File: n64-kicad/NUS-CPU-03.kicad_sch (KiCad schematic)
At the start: 1 part

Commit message: Update
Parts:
- added U4: ~, symbol n64:VDC-NUS
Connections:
- net +3V3: now also U4.1 (3V3)
- net GND: now also U4.12 (VSS), U4.9 (VSS)
- net at U1.11 (VIDEO_CLK): now also U4.11 (CLOCK)
- net at U1.14 (VIDEO_SYNC): now also U4.10 (~{DSYNC})
- net at U1.15 (VIDEO_D6): now also U4.8 (D6)
- net at U1.18 (VIDEO_D5): now also U4.7 (D5)
- net at U1.19 (VIDEO_D4): now also U4.6 (D4)
- net at U1.20 (VIDEO_D3): now also U4.5 (D3)
- net at U1.23 (VIDEO_D2): now also U4.4 (D2)
- net at U1.24 (VIDEO_D1): now also U4.3 (D1)
- net at U1.25 (VIDEO_D0): now also U4.2 (D0)
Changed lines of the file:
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@@
   (junction (at 165.1 93.98) (diameter 0) (color 0 0 0 0)
   )
+  (junction (at 219.71 124.46) (diameter 0) (color 0 0 0 0)
+  )
   (junction (at 157.48 160.02) (diameter 0) (color 0 0 0 0)
   )
@@
   (junction (at 162.56 86.36) (diameter 0) (color 0 0 0 0)
   )
+  (wire (pts (xy 190.5 116.84) (xy 190.5 111.76))
+    (stroke (width 0) (type default))
+  )
   (wire (pts (xy 165.1 88.9) (xy 165.1 93.98))
     (stroke (width 0) (type default))
   )
+  (wire (pts (xy 157.48 111.76) (xy 180.34 111.76))
+    (stroke (width 0) (type default))
+  )
+  (wire (pts (xy 195.58 124.46) (xy 157.48 124.46))
+    (stroke (width 0) (type default))
+  )
   (wire (pts (xy 157.48 91.44) (xy 162.56 91.44))
     (stroke (width 0) (type default))
@@
     (stroke (width 0) (type default))
   )
+  (wire (pts (xy 219.71 96.52) (xy 222.25 96.52))
+    (stroke (width 0) (type default))
+  )
   (wire (pts (xy 157.48 106.68) (xy 165.1 106.68))
     (stroke (width 0) (type default))
@@
     (stroke (width 0) (type default))
   )
+  (wire (pts (xy 157.48 101.6) (xy 222.25 101.6))
+    (stroke (width 0) (type default))
+  )
   (wire (pts (xy 165.1 106.68) (xy 165.1 119.38))
     (stroke (width 0) (type default))
@@
     (stroke (width 0) (type default))
   )
+  (wire (pts (xy 205.74 121.92) (xy 205.74 134.62))
+    (stroke (width 0) (type default))
+  )
+  (wire (pts (xy 219.71 124.46) (xy 222.25 124.46))
+    (stroke (width 0) (type default))
+  )
   (wire (pts (xy 162.56 121.92) (xy 162.56 109.22))
     (stroke (width 0) (type default))
   )
+  (wire (pts (xy 157.48 116.84) (xy 190.5 116.84))
+    (stroke (width 0) (type default))
+  )
   (wire (pts (xy 157.48 129.54) (xy 165.1 129.54))
     (stroke (width 0) (type default))
@@
     (stroke (width 0) (type default))
   )
+  (wire (pts (xy 219.71 124.46) (xy 219.71 127))
+    (stroke (width 0) (type default))
+  )
   (wire (pts (xy 157.48 93.98) (xy 165.1 93.98))
     (stroke (width 0) (type default))
   )
+  (wire (pts (xy 219.71 116.84) (xy 222.25 116.84))
+    (stroke (width 0) (type default))
+  )
   (wire (pts (xy 162.56 86.36) (xy 162.56 71.12))
     (stroke (width 0) (type default))
@@
     (stroke (width 0) (type default))
   )
+  (wire (pts (xy 222.25 109.22) (xy 185.42 109.22))
+    (stroke (width 0) (type default))
+  )
+  (wire (pts (xy 200.66 127) (xy 157.48 127))
+    (stroke (width 0) (type default))
+  )
   (wire (pts (xy 165.1 45.72) (xy 165.1 68.58))
     (stroke (width 0) (type default))
   )
+  (wire (pts (xy 185.42 109.22) (xy 185.42 114.3))
+    (stroke (width 0) (type default))
+  )
   (wire (pts (xy 157.48 142.24) (xy 162.56 142.24))
     (stroke (width 0) (type default))
@@
     (stroke (width 0) (type default))
   )
+  (wire (pts (xy 219.71 116.84) (xy 219.71 124.46))
+    (stroke (width 0) (type default))
+  )
+  (wire (pts (xy 222.25 121.92) (xy 205.74 121.92))
+    (stroke (width 0) (type default))
+  )
+  (wire (pts (xy 190.5 111.76) (xy 222.25 111.76))
+    (stroke (width 0) (type default))
+  )
   (wire (pts (xy 162.56 157.48) (xy 162.56 142.24))
     (stroke (width 0) (type default))
@@
     (stroke (width 0) (type default))
   )
+  (wire (pts (xy 222.25 119.38) (xy 200.66 119.38))
+    (stroke (width 0) (type default))
+  )
+  (wire (pts (xy 195.58 114.3) (xy 195.58 124.46))
+    (stroke (width 0) (type default))
+  )
   (wire (pts (xy 162.56 109.22) (xy 162.56 91.44))
     (stroke (width 0) (type default))
@@
     (stroke (width 0) (type default))
   )
+  (wire (pts (xy 180.34 106.68) (xy 222.25 106.68))
+    (stroke (width 0) (type default))
+  )
+  (wire (pts (xy 219.71 93.98) (xy 219.71 96.52))
+    (stroke (width 0) (type default))
+  )
+  (wire (pts (xy 222.25 114.3) (xy 195.58 114.3))
+    (stroke (width 0) (type default))
+  )
   (wire (pts (xy 165.1 68.58) (xy 165.1 88.9))
     (stroke (width 0) (type default))
@@
     (stroke (width 0) (type default))
   )
+  (wire (pts (xy 157.48 99.06) (xy 222.25 99.06))
+    (stroke (width 0) (type default))
+  )
+  (wire (pts (xy 200.66 119.38) (xy 200.66 127))
+    (stroke (width 0) (type default))
+  )
   (wire (pts (xy 157.48 139.7) (xy 165.1 139.7))
     (stroke (width 0) (type default))
   )
+  (wire (pts (xy 205.74 134.62) (xy 157.48 134.62))
+    (stroke (width 0) (type default))
+  )
+  (wire (pts (xy 157.48 104.14) (xy 222.25 104.14))
+    (stroke (width 0) (type default))
+  )
   (wire (pts (xy 157.48 88.9) (xy 165.1 88.9))
+    (stroke (width 0) (type default))
+  )
+  (wire (pts (xy 180.34 111.76) (xy 180.34 106.68))
+    (stroke (width 0) (type default))
+  )
+  (wire (pts (xy 185.42 114.3) (xy 157.48 114.3))
     (stroke (width 0) (type default))
   )
@@
     (effects (font (size 5.08 5.08)) (justify left bottom))
   )
-  (symbol (lib_id "power:+3V3") (at 165.1 45.72 0) (unit 1)
+  (symbol (lib_id "n64:VDC-NUS") (at 245.11 129.54 0) (unit 1)
+    (in_bom yes) (on_board yes) (dnp no)
+    (property "Reference" "U4" (at 241.3 128.27 0)
+      (effects (font (size 1.27 1.27)))
+    )
+    (property "Value" "~" (at 245.11 129.54 0)
+      (effects (font (size 1.27 1.27)))
+    )
+    (property "Footprint" "" (at 245.11 129.54 0)
+      (effects (font (size 1.27 1.27)) hide)
+    )
+    (property "Datasheet" "" (at 245.11 129.54 0)
+      (effects (font (size 1.27 1.27)) hide)
+    )
+    (pin "1")
+    (pin "10")
+    (pin "11")
+    (pin "12")
+    (pin "13")
+    (pin "14")
+    (pin "15")
+    (pin "16")
+    (pin "17")
+    (pin "18")
+    (pin "19")
+    (pin "2")
+    (pin "20")
+    (pin "21")
+    (pin "22")
+    (pin "23")
+    (pin "24")
+    (pin "3")
+    (pin "4")
+    (pin "5")
+    (pin "6")
+    (pin "7")
+    (pin "8")
+    (pin "9")
+    (instances
+      (project "n64-kicad"
+        (path "/62362fc5-d8b0-453c-8cf3-9bf5adb1c5ec/fe0f5ce9-be45-40ad-8b42-2b325418535e"
+          (reference "U4") (unit 1)
+        )
+      )
+    )
+  )
+  (symbol (lib_id "power:GND") (at 219.71 127 0) (unit 1)
     (in_bom yes) (on_board yes) (dnp no) (fields_autoplaced)
-    (property "Reference" "#PWR02" (at 165.1 49.53 0)
-      (effects (font (size 1.27 1.27)) hide)
-    )
-    (property "Value" "+3V3" (at 165.1 41.91 0)
-      (effects (font (size 1.27 1.27)))
-    )
-    (property "Footprint" "" (at 165.1 45.72 0)
-      (effects (font (size 1.27 1.27)) hide)
-    )
-    (property "Datasheet" "" (at 165.1 45.72 0)
+    (property "Reference" "#PWR01" (at 219.71 133.35 0)
+      (effects (font (size 1.27 1.27)) hide)
+    )
+    (property "Value" "GND" (at 219.71 132.08 0)
+      (effects (font (size 1.27 1.27)))
+    )
+    (property "Footprint" "" (at 219.71 127 0)
+      (effects (font (size 1.27 1.27)) hide)
+    )
+    (property "Datasheet" "" (at 219.71 127 0)
+      (effects (font (size 1.27 1.27)) hide)
+    )
+    (pin "1")
+    (instances
+      (project "n64-kicad"
+        (path "/62362fc5-d8b0-453c-8cf3-9bf5adb1c5ec"
+          (reference "#PWR01") (unit 1)
+        )
+        (path "/62362fc5-d8b0-453c-8cf3-9bf5adb1c5ec/702eb8d5-895e-4c34-90ce-20d99f2fa9dd"
+          (reference "#PWR01") (unit 1)
+        )
+        (path "/62362fc5-d8b0-453c-8cf3-9bf5adb1c5ec/2087c345-615f-4492-b530-065219fa6c1e"
+          (reference "#PWR05") (unit 1)
+        )
+        (path "/62362fc5-d8b0-453c-8cf3-9bf5adb1c5ec/fe0f5ce9-be45-40ad-8b42-2b325418535e"
+          (reference "#PWR011") (unit 1)
+        )
+      )
+    )
+  )
+  (symbol (lib_id "power:+3V3") (at 219.71 93.98 0) (unit 1)
+    (in_bom yes) (on_board yes) (dnp no) (fields_autoplaced)
+    (property "Reference" "#PWR02" (at 219.71 97.79 0)
+      (effects (font (size 1.27 1.27)) hide)
+    )
+    (property "Value" "+3V3" (at 219.71 90.17 0)
+      (effects (font (size 1.27 1.27)))
+    )
+    (property "Footprint" "" (at 219.71 93.98 0)
+      (effects (font (size 1.27 1.27)) hide)
+    )
+    (property "Datasheet" "" (at 219.71 93.98 0)
       (effects (font (size 1.27 1.27)) hide)
     )
@@
         )
         (path "/62362fc5-d8b0-453c-8cf3-9bf5adb1c5ec/fe0f5ce9-be45-40ad-8b42-2b325418535e"
+          (reference "#PWR012") (unit 1)
+        )
+      )
+    )
+  )
+  (symbol (lib_id "power:+3V3") (at 165.1 45.72 0) (unit 1)
+    (in_bom yes) (on_board yes) (dnp no) (fields_autoplaced)
+    (property "Reference" "#PWR02" (at 165.1 49.53 0)
+      (effects (font (size 1.27 1.27)) hide)
+    )
+    (property "Value" "+3V3" (at 165.1 41.91 0)
+      (effects (font (size 1.27 1.27)))
+    )
+    (property "Footprint" "" (at 165.1 45.72 0)
+      (effects (font (size 1.27 1.27)) hide)
+    )
+    (property "Datasheet" "" (at 165.1 45.72 0)
+      (effects (font (size 1.27 1.27)) hide)
+    )
+    (pin "1")
+    (instances
+      (project "n64-kicad"
+        (path "/62362fc5-d8b0-453c-8cf3-9bf5adb1c5ec"
+          (reference "#PWR02") (unit 1)
+        )
+        (path "/62362fc5-d8b0-453c-8cf3-9bf5adb1c5ec/702eb8d5-895e-4c34-90ce-20d99f2fa9dd"
+          (reference "#PWR02") (unit 1)
+        )
+        (path "/62362fc5-d8b0-453c-8cf3-9bf5adb1c5ec/2087c345-615f-4492-b530-065219fa6c1e"
+          (reference "#PWR06") (unit 1)
+        )
+        (path "/62362fc5-d8b0-453c-8cf3-9bf5adb1c5ec/fe0f5ce9-be45-40ad-8b42-2b325418535e"
           (reference "#PWR010") (unit 1)
         )
@@
   (symbol (lib_id "n64:RCP-NUS") (at 152.4 185.42 0) (unit 1)
     (in_bom yes) (on_board yes) (dnp no)
-    (property "Reference" "U1" (at 149.86 172.72 0)
+    (property "Reference" "U1" (at 151.13 172.72 0)
       (effects (font (size 1.27 1.27)))
     )
@@
         )
         (path "/62362fc5-d8b0-453c-8cf3-9bf5adb1c5ec/fe0f5ce9-be45-40ad-8b42-2b325418535e"
-          (reference "U6") (unit 1)
+          (reference "U9") (unit 1)
         )
       )

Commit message: Update
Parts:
- added U6: ~, symbol n64:PIF-NUS
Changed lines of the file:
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@@
+    )
+  )
+  (symbol (lib_id "n64:PIF-NUS") (at 297.18 201.93 0) (unit 1)
+    (in_bom yes) (on_board yes) (dnp no)
+    (property "Reference" "U6" (at 295.91 200.66 0)
+      (effects (font (size 1.27 1.27)))
+    )
+    (property "Value" "~" (at 297.18 201.93 0)
+      (effects (font (size 1.27 1.27)))
+    )
+    (property "Footprint" "" (at 297.18 201.93 0)
+      (effects (font (size 1.27 1.27)) hide)
+    )
+    (property "Datasheet" "" (at 297.18 201.93 0)
+      (effects (font (size 1.27 1.27)) hide)
+    )
+    (pin "1")
+    (pin "10")
+    (pin "11")
+    (pin "12")
+    (pin "13")
+    (pin "14")
+    (pin "15")
+    (pin "16")
+    (pin "17")
+    (pin "18")
+    (pin "19")
+    (pin "2")
+    (pin "20")
+    (pin "21")
+    (pin "22")
+    (pin "23")
+    (pin "24")
+    (pin "25")
+    (pin "26")
+    (pin "27")
+    (pin "28")
+    (pin "3")
+    (pin "4")
+    (pin "5")
+    (pin "6")
+    (pin "7")
+    (pin "8")
+    (pin "9")
+    (instances
+      (project "n64-kicad"
+        (path "/62362fc5-d8b0-453c-8cf3-9bf5adb1c5ec/fe0f5ce9-be45-40ad-8b42-2b325418535e"
+          (reference "U6") (unit 1)
+        )
+      )
     )
   )

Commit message: Add CPU-NUS
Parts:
- added U10: CPU-NUS, symbol n64:CPU-NUS
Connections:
- net +3V3: now also U1.101 (VCC), U1.106 (VCC), U1.110 (VCC), U1.114 (VCC), U1.120 (VCC), U1.126 (VCC), U1.130 (VCC), U1.147 (VCC), U1.148 (VCC), U1.152 (VCC), U1.43 (VCC), U1.49 (VCC), U1.56 (VCC), U1.64 (VCC), U1.71 (VCC), U1.77 (VCC), U1.83 (VCC), U1.88 (VCC), U1.90 (VCC), U1.98 (VCC)
- net GND: now also U1.100 (VSS), U1.105 (VSS), U1.109 (VSS), U1.113 (VSS), U1.119 (VSS), U1.125 (VSS), U1.128 (VSS), U1.132 (VSS), U1.134 (VSS), U1.136 (VSS), U1.138 (VSS), U1.140 (VSS), U1.142 (VSS), U1.145 (VSS), U1.150 (VSS), U1.154 (VSS), U1.156 (VSS), U1.158 (VSS), U1.160 (VSS), U1.42 (VSS), U1.48 (VSS), U1.55 (VSS), U1.63 (VSS), U1.70 (VSS), U1.76 (VSS), U1.82 (VSS), U1.89 (VSS), U1.91 (VSS), U1.97 (VSS)
- net ~{VideoDSync}: now reaches U1.14 (~{VIDEO_DSYNC}), U4.10 (~{DSYNC})
- net VideoClk: now reaches U1.11 (VIDEO_CLK), U4.11 (CLOCK)
- net VideoD0: now reaches U1.25 (VIDEO_D0), U4.2 (D0)
- net VideoD1: now reaches U1.24 (VIDEO_D1), U4.3 (D1)
- net VideoD2: now reaches U1.23 (VIDEO_D2), U4.4 (D2)
- net VideoD3: now reaches U1.20 (VIDEO_D3), U4.5 (D3)
- net VideoD4: now reaches U1.19 (VIDEO_D4), U4.6 (D4)
- net VideoD5: now reaches U1.18 (VIDEO_D5), U4.7 (D5)
- net VideoD6: now reaches U1.15 (VIDEO_D6), U4.8 (D6)
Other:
- moved on the sheet: U1, U4, U6

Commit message: Split up CPU-NUS
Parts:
- removed U10: CPU-NUS, symbol n64:CPU-NUS
- added C5, C6, C7, C8, C9: ? nF, symbol Device:C_Small
- added R29, R30: 4k7, symbol Device:R_Small
- added U8: CPU-NUS, symbol n64:CPU-NUS_split
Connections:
- net +3V3: now also R29.1, U8.1 (VDD), U8.101 (VDD), U8.105 (~{Reset}), U8.107 (VDD), U8.112 (DivMode0), U8.113 (VDD), U8.118 (~{Int3}), U8.119 (VDD), U8.15 (VDD(DivMode2)), U8.19 (VDD), U8.23 (VDD), U8.29 (VDD), U8.32 (VDD), U8.36 (VDD), U8.40 (VDD), U8.44 (VDD), U8.49 (VDD), U8.5 (VDD), U8.52 (JTMS), U8.54 (VDD), U8.57 (~{Int1}), U8.58 (JTCK), U8.62 (VDD), U8.63 (JTDI), U8.68 (VDD), U8.72 (VDD), U8.76 (VDD), U8.80 (VDD), U8.85 (VDD), U8.90 (VDD), U8.92 (VDD), U8.96 (VDD)
- net GND: now also R30.2, U8.102 (GND), U8.108 (GND), U8.114 (GND), U8.116 (DivMode1), U8.120 (GND), U8.17 (GND), U8.2 (GND), U8.20 (GND), U8.25 (GND), U8.30 (GND), U8.31 (GND), U8.35 (GND), U8.39 (GND), U8.43 (GND), U8.48 (GND), U8.53 (GND), U8.59 (GND), U8.6 (GND), U8.60 (VDD), U8.61 (GND), U8.67 (GND), U8.71 (GND), U8.75 (GND), U8.79 (GND), U8.8 (GND), U8.84 (GND), U8.89 (GND), U8.91 (GND), U8.97 (GND)
- new net: C5.1, C8.1, C9.1, R29.2, U8.13 (VDDP), U8.9 (VDDP)
- new net: C5.2, C6.2, C7.2, C8.2, C9.2, R30.1, U8.10 (GNDP), U8.14 (GNDP)
- new net: C7.1, U8.12 (PLLCAP1)
- new net: U8.21 (SyncOut), U8.24 (SyncIn)
- new net: C6.1, U8.11 (PLLCAP0)
- new net MasterClock: U8.16 (MasterClock)
- new net SysAD0: U8.73 (SysAD0)
- new net SysAD1: U8.70 (SysAD1)
- new net SysAD10: U8.45 (SysAD10)
- new net SysAD11: U8.42 (SysAD11)
- new net SysAD12: U8.41 (SysAD12)
- new net SysAD13: U8.38 (SysAD13)
- new net SysAD14: U8.37 (SysAD14)
- new net SysAD15: U8.34 (SysAD15)
- new net SysAD16: U8.33 (SysAD16)
- new net SysAD17: U8.27 (SysAD17)
- new net SysAD18: U8.26 (SysAD18)
- new net SysAD19: U8.22 (SysAD19)
- new net SysAD2: U8.69 (SysAD2)
- new net SysAD20: U8.7 (SysAD20)
- new net SysAD21: U8.4 (SysAD21)
- new net SysAD22: U8.3 (SysAD22)
- new net SysAD23: U8.117 (SysAD23)
- new net SysAD24: U8.115 (SysAD24)
- new net SysAD25: U8.98 (SysAD25)
- new net SysAD26: U8.94 (SysAD26)
- new net SysAD27: U8.87 (SysAD27)
- new net SysAD28: U8.86 (SysAD28)
- new net SysAD29: U8.83 (SysAD29)
- new net SysAD3: U8.66 (SysAD3)
- new net SysAD30: U8.81 (SysAD30)
- new net SysAD31: U8.77 (SysAD31)
- new net SysAD4: U8.64 (SysAD4)
- new net SysAD5: U8.56 (SysAD5)
- new net SysAD6: U8.55 (SysAD6)
- new net SysAD7: U8.51 (SysAD7)
- new net SysAD8: U8.50 (SysAD8)
- new net SysAD9: U8.47 (SysAD9)
- new net SysCmd0: U8.100 (SysCmd0)
- new net SysCmd1: U8.103 (SysCmd1)
- new net SysCmd2: U8.106 (SysCmd2)
- new net SysCmd3: U8.109 (SysCmd3)
- new net SysCmd4: U8.111 (SysCmd4)
- new net ~{ColdReset}: U8.110 (~{ColdReset})
- new net ~{EOK}: U8.82 (~{EOK})
- new net ~{EReq}: U8.99 (~{EReq})
- new net ~{EValid}: U8.104 (~{EValid})
- new net ~{Int0}: U8.46 (~{Int0})
- new net ~{Int2}: U8.88 (~{Int2})
- new net ~{Int4}: U8.28 (~{Int4})
- new net ~{NMI}: U8.93 (~{NMI})
- new net ~{PValid}: U8.78 (~{PValid})
- no-connect marks 0 -> 4
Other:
- moved on the sheet: U1, U4, U6

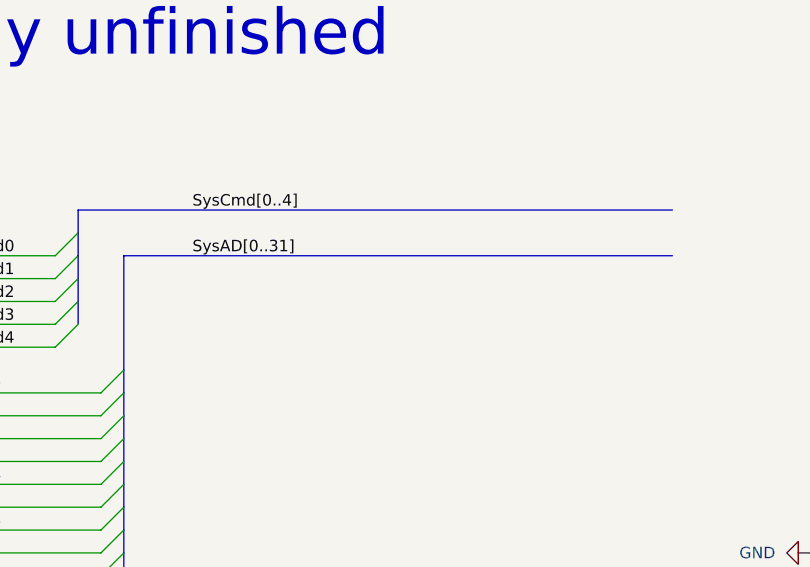
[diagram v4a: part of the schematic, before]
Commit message: Add warning note about kicad crash
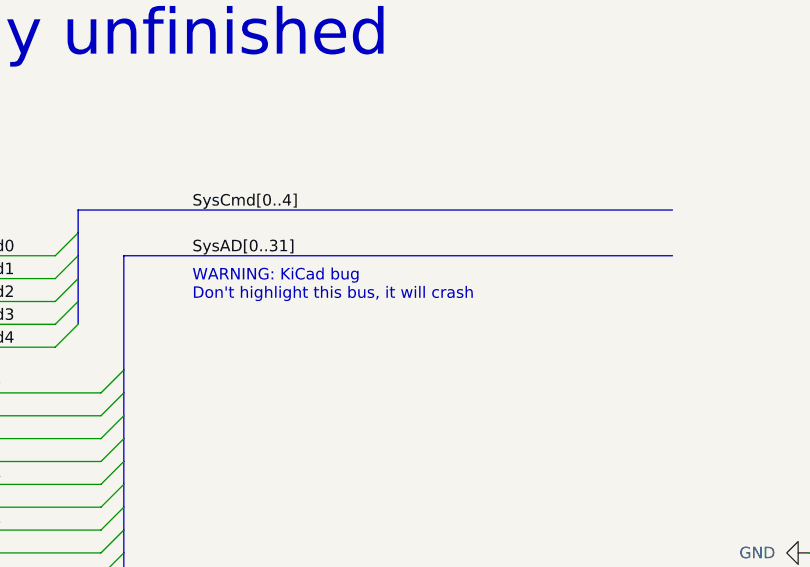
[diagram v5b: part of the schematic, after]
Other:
- note added: "WARNING: KiCad bug Don't highlight this bus, it will crash"
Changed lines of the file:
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@@
     (effects (font (size 5.08 5.08)) (justify left bottom))
+  )
+  (text "WARNING: KiCad bug\nDon't highlight this bus, it will crash"
+    (at 223.52 53.34 0)
+    (effects (font (size 1.27 1.27)) (justify left bottom))
   )
   (text "NUS-CPU-03" (at 45.72 25.4 0)

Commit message: RAM
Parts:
- added P1: Expansion Pak Connector, symbol Connector_Generic:Conn_01x36
- added U11, U14: RDRAM18-NUS, symbol n64:RDRAM18-NUS
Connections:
- net +3V3: now also P1.10 (Pin_10), P1.14 (Pin_14), P1.18 (Pin_18), P1.34 (Pin_34), P1.4 (Pin_4), U11.1 (VDD), U11.12 (VDDA), U11.16 (VDD), U11.32 (VDD), U11.8 (VDD), U14.1 (VDD), U14.12 (VDDA), U14.16 (VDD), U14.20 (SIN), U14.32 (VDD), U14.8 (VDD)
- net GND: now also P1.12 (Pin_12), P1.16 (Pin_16), P1.2 (Pin_2), P1.20 (Pin_20), P1.22 (Pin_22), P1.24 (Pin_24), P1.26 (Pin_26), P1.30 (Pin_30), P1.32 (Pin_32), P1.36 (Pin_36), P1.6 (Pin_6), U11.10 (GND), U11.14 (GNDA), U11.18 (GND), U11.2 (GND), U11.24 (GND), U11.28 (GND), U11.30 (NC/GND), U11.31 (GND), U11.4 (GND), U14.10 (GND), U14.14 (GNDA), U14.18 (GND), U14.2 (GND), U14.24 (GND), U14.28 (GND), U14.30 (NC/GND), U14.31 (GND), U14.4 (GND)
- new net: P1.33 (Pin_33), U11.22 (SOUT)
- new net ExpansionPakCLK: P1.3 (Pin_3)
- new net Ram1SOut: U11.20 (SIN), U14.22 (SOUT)
- new net RamAddr: P1.9 (Pin_9), U11.7 (ADDR), U14.7 (ADDR)
- new net RamCmd: P1.21 (Pin_21), U11.19 (CMD), U14.19 (CMD)
- new net RamDQ0: P1.31 (Pin_31), U11.29 (DQ0), U14.29 (DQ0)
- new net RamDQ1: P1.29 (Pin_29), U11.27 (DQ1), U14.27 (DQ1)
- new net RamDQ2: P1.27 (Pin_27), U11.25 (DQ2), U14.25 (DQ2)
- new net RamDQ3: P1.25 (Pin_25), U11.23 (DQ3), U14.23 (DQ3)
- new net RamDQ4: P1.19 (Pin_19), U11.17 (DQ4), U14.17 (DQ4)
- new net RamDQ5: P1.13 (Pin_13), U11.11 (DQ5), U14.11 (DQ5)
- new net RamDQ6: P1.11 (Pin_11), U11.9 (DQ6), U14.9 (DQ6)
- new net RamDQ7: P1.7 (Pin_7), U11.5 (DQ7), U14.5 (DQ7)
- new net RamDQ8: P1.5 (Pin_5), U11.3 (DQ8), U14.3 (DQ8)
- new net RamRxClk: P1.15 (Pin_15), U11.13 (RXCLK), U14.13 (RXCLK)
- new net RamTxClk: P1.17 (Pin_17), U11.15 (TXCLK), U14.15 (TXCLK)
- new net VRef: P1.23 (Pin_23), U11.21 (VREF(1.92V)), U14.21 (VREF(1.92V))
- new net VTerm: P1.28 (Pin_28), P1.8 (Pin_8)
- no-connect marks 4 -> 6
